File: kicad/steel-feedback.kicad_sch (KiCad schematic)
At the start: 119 parts, among them J1 AudioJack2_SwitchT, J2 AudioJack2_SwitchT, J4 AudioJack2_SwitchT, J5 AudioJack2_SwitchT, J6 AudioJack2_SwitchT, J7 AudioJack2_SwitchT, Q1 2N3904, Q2 2N3906, Q3 2N3906, SW2 SW_SPDT, SW3 SW_SPDT, U10 TL072, U11 TL072, U12 TL072, U13 TL072, U2 LM13700, U3 LM13700, U4 TL072, U5 TL072, U6 LM386, U7 NE5534, U8 TL072

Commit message: Tweaking values now that build is in progress
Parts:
- removed LS1: Speaker, KK254_Horizontal:Molex_KK-254_1x02_P2.54mm_Horizontal, symbol Device:Speaker
- removed MK1: Piezo, KK254_Horizontal:Molex_KK-254_1x02_P2.54mm_Horizontal, symbol Rumblesan_Standard_Parts:Piezo
- added H1, H2, H3, H4: MountingHole_Pad, MountingHole:MountingHole_3.2mm_M3_Pad, symbol Mechanical:MountingHole_Pad
- added J10, J9: Conn_01x02, Rumblesan_Connectors:Molex_KK-254_22-05-7028_1x02_P2.54mm_Horizontal, symbol Connector_Generic:Conn_01x02
- C1, C2, C3: value 100pF -> 150pF
- C35: value 20pF -> 22pF
- C41: value 33nF -> 47nF
- C9: value 220uF -> 100uF
- JP1: now left out of the parts list
- R25: value 56k -> 68k
- R29: value 2k2 -> 2k
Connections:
- net GND: now also H1.1, H2.1, H3.1, H4.1, J9.2 (Pin_2)
- net VEE: now also J10.1 (Pin_1)
- net at D1.2 (A), D2.1 (K), R47.2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: now also J10.2 (Pin_2)
- net at C9.2: now also J9.1 (Pin_1)
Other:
- note added: "Piezo"
- note added: "Speaker"
- moved on the sheet: R35

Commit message: Fixing issues in schematic
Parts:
- R18: value 10k -> 22k
- R25: value 68k -> 47k
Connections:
- net GND: now also J10.1 (Pin_1), R47.2
- net VCC: no longer R47.1
- net VEE: no longer J10.1 (Pin_1)
- net at D1.2 (A), D2.1 (K), J10.2 (Pin_2)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: now also R47.1; no longer R47.2
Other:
- moved on the sheet: J10, R47
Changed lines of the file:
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@@
 	)
 	(junction
+		(at 186.69 190.5)
+		(diameter 0)
+		(color 0 0 0 0)
+	)
+	(junction
 		(at 99.06 119.38)
 		(diameter 0)
@@
 	)
 	(junction
-		(at 189.23 190.5)
-		(diameter 0)
-		(color 0 0 0 0)
-	)
-	(junction
 		(at 50.8 97.79)
 		(diameter 0)
@@
 	(wire
 		(pts
-			(xy 189.23 186.69) (xy 189.23 190.5)
-		)
-		(stroke
-			(width 0)
-			(type default)
-		)
-	)
-	(wire
-		(pts
 			(xy 113.03 130.81) (xy 114.3 130.81)
 		)
@@
 	(wire
 		(pts
-			(xy 189.23 190.5) (xy 204.47 190.5)
+			(xy 173.99 190.5) (xy 186.69 190.5)
 		)
 		(stroke
@@
 	(wire
 		(pts
-			(xy 189.23 190.5) (xy 189.23 198.12)
-		)
-		(stroke
-			(width 0)
-			(type default)
-		)
-	)
-	(wire
-		(pts
 			(xy 320.04 130.81) (xy 320.04 121.92)
 		)
@@
 	(wire
 		(pts
+			(xy 186.69 190.5) (xy 204.47 190.5)
+		)
+		(stroke
+			(width 0)
+			(type default)
+		)
+	)
+	(wire
+		(pts
 			(xy 290.83 215.9) (xy 289.56 215.9)
 		)
@@
 	(wire
 		(pts
-			(xy 184.15 200.66) (xy 189.23 200.66)
+			(xy 175.26 193.04) (xy 173.99 193.04)
 		)
 		(stroke
@@
 	(wire
 		(pts
-			(xy 189.23 176.53) (xy 189.23 179.07)
-		)
-		(stroke
-			(width 0)
-			(type default)
-		)
-	)
-	(wire
-		(pts
 			(xy 53.34 195.58) (xy 53.34 201.93)
 		)
@@
 	(wire
 		(pts
-			(xy 189.23 200.66) (xy 189.23 207.01)
+			(xy 175.26 193.04) (xy 175.26 199.39)
 		)
 		(stroke
@@
 	(wire
 		(pts
-			(xy 184.15 198.12) (xy 189.23 198.12)
-		)
-		(stroke
-			(width 0)
-			(type default)
-		)
-	)
-	(wire
-		(pts
 			(xy 154.94 93.98) (xy 146.05 93.98)
 		)
@@
 	(wire
 		(pts
+			(xy 186.69 200.66) (xy 186.69 201.93)
+		)
+		(stroke
+			(width 0)
+			(type default)
+		)
+	)
+	(wire
+		(pts
 			(xy 58.42 195.58) (xy 53.34 195.58)
 		)
@@
 	(wire
 		(pts
+			(xy 186.69 190.5) (xy 186.69 193.04)
+		)
+		(stroke
+			(width 0)
+			(type default)
+		)
+	)
+	(wire
+		(pts
 			(xy 302.26 128.27) (xy 303.53 128.27)
 		)
@@
 	(text "Piezo"
 		(exclude_from_sim no)
-		(at 173.736 199.898 0)
+		(at 163.576 192.278 0)
 		(effects
 			(font
@@
 	)
 	(symbol
+		(lib_id "power:GND")
+		(at 175.26 199.39 0)
+		(mirror y)
+		(unit 1)
+		(exclude_from_sim no)
+		(in_bom yes)
+		(on_board yes)
+		(dnp no)
+		(fields_autoplaced yes)
+		(property "Reference" "#PWR050"
+			(at 175.26 205.74 0)
+			(effects
+				(font
+					(size 1.27 1.27)
+				)
+				(hide yes)
+			)
+		)
+		(property "Value" "GND"
+			(at 175.26 204.47 0)
+			(effects
+				(font
+					(size 1.27 1.27)
+				)
+			)
+		)
+		(property "Footprint" ""
+			(at 175.26 199.39 0)
+			(effects
+				(font
+					(size 1.27 1.27)
+				)
+				(hide yes)
+			)
+		)
+		(property "Datasheet" ""
+			(at 175.26 199.39 0)
+			(effects
+				(font
+					(size 1.27 1.27)
+				)
+				(hide yes)
+			)
+		)
+		(property "Description" "Power symbol creates a global label with name \"GND\" , ground"
+			(at 175.26 199.39 0)
+			(effects
+				(font
+					(size 1.27 1.27)
+				)
+				(hide yes)
+			)
+		)
+		(pin "1"
+		)
+		(instances
+			(project "steel-feedback"
+				(path "/5b0acaca-dc50-4fa5-b146-164c1b9ad031"
+					(reference "#PWR050")
+					(unit 1)
+				)
+			)
+		)
+	)
+	(symbol
 		(lib_id "power:VEE")
 		(at 217.17 203.2 180)
@@
 	)
 	(symbol
-		(lib_id "power:VCC")
-		(at 189.23 176.53 0)
-		(mirror y)
-		(unit 1)
-		(exclude_from_sim no)
-		(in_bom yes)
-		(on_board yes)
-		(dnp no)
-		(fields_autoplaced yes)
-		(property "Reference" "#PWR049"
-			(at 189.23 180.34 0)
-			(effects
-				(font
-					(size 1.27 1.27)
-				)
-				(hide yes)
-			)
-		)
-		(property "Value" "VCC"
-			(at 189.23 171.45 0)
-			(effects
-				(font
-					(size 1.27 1.27)
-				)
-			)
-		)
-		(property "Footprint" ""
-			(at 189.23 176.53 0)
-			(effects
-				(font
-					(size 1.27 1.27)
-				)
-				(hide yes)
-			)
-		)
-		(property "Datasheet" ""
-			(at 189.23 176.53 0)
-			(effects
-				(font
-					(size 1.27 1.27)
-				)
-				(hide yes)
-			)
-		)
-		(property "Description" "Power symbol creates a global label with name \"VCC\""
-			(at 189.23 176.53 0)
-			(effects
-				(font
-					(size 1.27 1.27)
-				)
-				(hide yes)
-			)
-		)
-		(pin "1"
-		)
-		(instances
-			(project "steel-feedback"
-				(path "/5b0acaca-dc50-4fa5-b146-164c1b9ad031"
-					(reference "#PWR049")
-					(unit 1)
-				)
-			)
-		)
-	)
-	(symbol
 		(lib_id "power:GND")
 		(at 184.15 69.85 0)
@@
 			)
 		)
-		(property "Value" "68k"
+		(property "Value" "47k"
 			(at 147.32 45.72 90)
 			(effects
@@
 			)
 		)
-		(property "Value" "10k"
+		(property "Value" "22k"
 			(at 342.9 138.4299 0)
 			(effects
@@
 	(symbol
 		(lib_id "Connector_Generic:Conn_01x02")
-		(at 179.07 200.66 180)
+		(at 168.91 193.04 180)
 		(unit 1)
 		(exclude_from_sim no)
@@
 		(dnp no)
 		(property "Reference" "J10"
-			(at 179.07 195.072 0)
+			(at 168.91 187.452 0)
 			(effects
 				(font
@@
 		)
 		(property "Value" "Conn_01x02"
-			(at 179.07 204.47 0)
+			(at 168.91 196.85 0)
 			(effects
 				(font
@@
 		)
 		(property "Footprint" "Rumblesan_Connectors:Molex_KK-254_22-05-7028_1x02_P2.54mm_Horizontal"
-			(at 179.07 200.66 0)
+			(at 168.91 193.04 0)
 			(effects
 				(font
@@
 		)
 		(property "Datasheet" "~"
-			(at 179.07 200.66 0)
+			(at 168.91 193.04 0)
 			(effects
 				(font
@@
 		)
 		(property "Description" "Generic connector, single row, 01x02, script generated (kicad-library-utils/schlib/autogen/connector/)"
-			(at 179.07 200.66 0)
+			(at 168.91 193.04 0)
 			(effects
 				(font
@@
 	)
 	(symbol
-		(lib_id "power:VEE")
-		(at 189.23 207.01 180)
+		(lib_id "power:GND")
+		(at 186.69 201.93 0)
+		(mirror y)
 		(unit 1)
 		(exclude_from_sim no)
@@
 		(dnp no)
 		(fields_autoplaced yes)
-		(property "Reference" "#PWR050"
-			(at 189.23 203.2 0)
+		(property "Reference" "#PWR049"
+			(at 186.69 208.28 0)
 			(effects
 				(font
@@
 			)
 		)
-		(property "Value" "VEE"
-			(at 189.23 212.09 0)
+		(property "Value" "GND"
+			(at 186.69 207.01 0)
 			(effects
 				(font
@@
 		)
 		(property "Footprint" ""
-			(at 189.23 207.01 0)
+			(at 186.69 201.93 0)
 			(effects
 				(font
@@
 		)
 		(property "Datasheet" ""
-			(at 189.23 207.01 0)
+			(at 186.69 201.93 0)
 			(effects
 				(font
@@
 			)
 		)
-		(property "Description" "Power symbol creates a global label with name \"VEE\""
-			(at 189.23 207.01 0)
+		(property "Description" "Power symbol creates a global label with name \"GND\" , ground"
+			(at 186.69 201.93 0)
 			(effects
 				(font
@@
 			(project "steel-feedback"
 				(path "/5b0acaca-dc50-4fa5-b146-164c1b9ad031"
-					(reference "#PWR050")
+					(reference "#PWR049")
 					(unit 1)
 				)
@@
 	(symbol
 		(lib_id "Rumblesan_Standard_Parts:R")
-		(at 189.23 182.88 0)
+		(at 186.69 196.85 0)
 		(mirror y)
 		(unit 1)
@@
 		(dnp no)
 		(property "Reference" "R47"
-			(at 186.69 181.6099 0)
+			(at 184.15 195.5799 0)
 			(effects
 				(font
@@
 		)
 		(property "Value" "1m"
-			(at 186.69 184.1499 0)
+			(at 184.15 198.1199 0)
 			(effects
 				(font
@@
 		)
 		(property "Footprint" "Rumblesan_Standard_Parts:R_Axial_DIN0207_L6.3mm_D2.5mm_P10.16mm_Horizontal"
-			(at 186.69 185.42 90)
+			(at 184.15 199.39 90)
 			(effects
 				(font
@@
 		)
 		(property "Datasheet" "~"
-			(at 182.88 182.88 90)
+			(at 180.34 196.85 90)
 			(effects
 				(font
@@
 		)
 		(property "Description" "Resistor"
-			(at 189.23 182.88 0)
+			(at 186.69 196.85 0)
 			(effects
 				(font
@@
 		)
 		(property "Tolerance" "1%"
-			(at 184.15 189.23 90)
+			(at 181.61 203.2 90)
 			(effects
 				(font
@@
 		)
 		(property "Power" "0.5W"
-			(at 184.15 175.26 90)
+			(at 181.61 189.23 90)
 			(effects
 				(font
@@
 		)
 		(property "Spec" "metal film"
-			(at 184.15 182.88 90)
+			(at 181.61 196.85 90)
 			(effects
 				(font

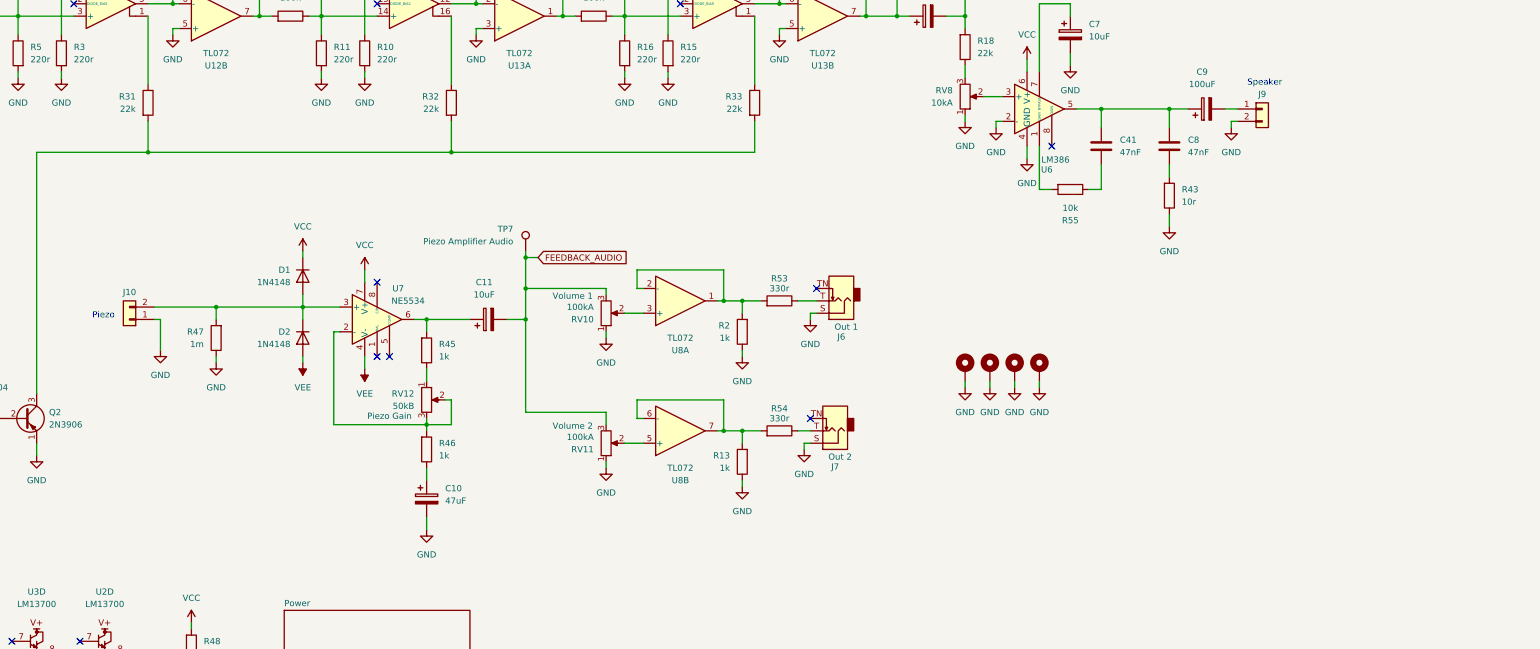
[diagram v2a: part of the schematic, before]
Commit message: Adding piezo and surface transducer to schematic
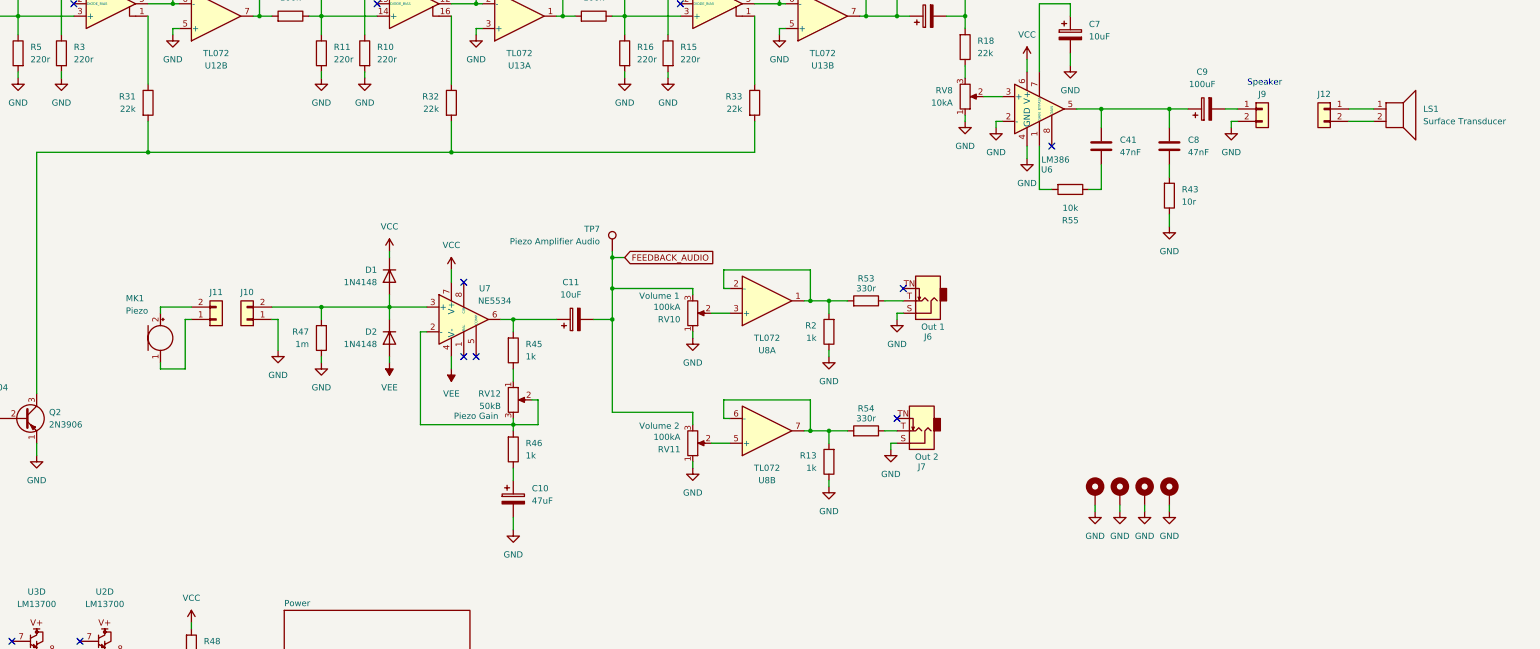
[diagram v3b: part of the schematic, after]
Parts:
- added J11, J12: Conn_01x02, Rumblesan_Connectors:Molex_KK-254_22-05-7028_1x02_P2.54mm_Horizontal, symbol Connector_Generic:Conn_01x02
- added LS1: Surface Transducer, symbol Device:Speaker
- added MK1: Piezo, Connector_PinHeader_2.54mm:PinHeader_1x02_P2.54mm_Vertical, symbol Rumblesan_Standard_Parts:Piezo
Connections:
- new net: J11.1 (Pin_1), MK1.1 (-)
- new net: J11.2 (Pin_2), MK1.2 (+)
- new net: J12.1 (Pin_1), LS1.1
- new net: J12.2 (Pin_2), LS1.2
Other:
- note removed: "Piezo"
- moved on the sheet: C10, C11, D1, D2, J10, J6, J7, R13, R2, R45, R46, R47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
